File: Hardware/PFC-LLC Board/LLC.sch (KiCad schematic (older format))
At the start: 49 parts

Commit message: Updated LLC schematic
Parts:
- removed C?: C, symbol Device:C
- removed Q? (x3): BF545A, Package_TO_SOT_SMD:SOT-23, symbol Transistor_FET:BF545A
- removed U?: UCC28180DR, D8_TEX, symbol PFC_IC:UCC28180DR
- added J2, J3: Conn_01x02_Female, Connector_PinHeader_1.27mm:PinHeader_1x02_P1.27mm_Vertical, symbol Connector:Conn_01x02_Female
- added QM1, QM2: IPP060N06N, Package_TO_SOT_THT:TO-220-3_Vertical, symbol Transistor_FET:IPP060N06N
- added QM3, QM4: C2M0025120D, Package_TO_SOT_THT:TO-247-3_Vertical, symbol Transistor_FET:C2M0025120D
- added Rlimit: 18.2k, symbol Device:R
- added U1: UCC256403DDBR, SOIC14_DDB_TEX, symbol LLC_U1:UCC256403DDBR
- added U2: UCC24624DT, SOIC_4624DT_TEX, symbol LLC_U2:UCC24624DT
- added UO1: PS2501L-1-F3-A, SOIC_1L-1-A, symbol LLC_O1:PS2501L-1-F3-A
- added UVR: TLV431AIDBVT, DBV5, symbol LLC_VR:TLV431AIDBVT
- Cboot: renamed from C?; value C -> 220n
- Cbw: renamed from C?; value C -> 3.9p
- Ccomp: renamed from C?; value C -> 390n
- Cisns: renamed from C?; value C -> 3.3p
- Cout: renamed from C?; value CP -> 120u
- Coutx: renamed from C?; value C -> 22u
- Creg, Cvcc: renamed from C?; value C -> 2.2u
- Crvcc2, Cvrcc1: renamed from C?; value C -> 4.7u
- Css: renamed from C?; value C -> 47n
- Cvcc2: renamed from C?; value CP -> 15u
- Cz: renamed from C?; value C -> 100n
- Rbias: renamed from R?; value R -> 6.04k
- Rboot: renamed from R?; value R -> 2.20
- Rcomp, Rvcc1: renamed from R?; value R -> 44.2k
- Rfbb: renamed from R?; value R -> 8.06k
- Rfbt: renamed from R?; value R -> 110k
- Rled: renamed from R?; value R -> 36.5k
- Rvcc2: renamed from R?; value R -> 12.1k
- gave numbers to parts that had none: 1
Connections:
- net labels added: BLK, GND, HO, HS, LO
- wire segments 64 -> 242
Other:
- moved on the sheet: C16, Cboot, Cbw, Ccomp, Cisns, Cout, Coutx, Creg, Crvcc2, Css, Cvcc, Cvrcc1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

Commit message: Start of PCB
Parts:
- removed Cout: 120u, symbol Device:CP
- removed Css: 47n, symbol Device:C
- removed Cvcc2: 15u, symbol Device:CP
- removed Cvcr2: 1n, symbol Device:C
- removed D?: DIODE, symbol pspice:DIODE
- added Cout21, Cout22, Cout23, Cout24, Cout25, Cout26: 120u, LLC_Cout:35SVPF120M, symbol LLC_Cout:35SVPF120M
- added Coutx21, Coutx23, Coutx24: 22u, Capacitor_SMD:C_0805_2012Metric_Pad1.18x1.45mm_HandSolder, symbol Device:C
- added Css11, Css12, Css13: 47n, Capacitor_SMD:C_0402_1005Metric_Pad0.74x0.62mm_HandSolder, symbol Device:C
- added Cvcc21, Cvcc22, Cvcc23, Cvcc24, Cvcc25, Cvcc26, Cvcc27, Cvcc28: 15u, Capacitor_SMD:CP_Elec_5x5.8, symbol Device:CP
- added Cvcr21, Cvcr22, Cvcr23, Cvcr24, Cvcr25, Cvcr26: 1n, Capacitor_SMD:C_0805_2012Metric_Pad1.18x1.45mm_HandSolder, symbol Device:C
- added Dz1: BZX84Cxx, Diode_SMD:D_SOT-23_ANK, symbol Diode:BZX84Cxx
- C16: footprint (none) -> Capacitor_SMD:C_0402_1005Metric_Pad0.74x0.62mm_HandSolder
- Cboot1: renamed from Cboot; footprint (none) -> Capacitor_SMD:C_0603_1608Metric_Pad1.08x0.95mm_HandSolder
- Cbw1: renamed from Cbw; footprint (none) -> Capacitor_SMD:C_0402_1005Metric_Pad0.74x0.62mm_HandSolder
- Ccomp3: renamed from Ccomp; footprint (none) -> Capacitor_SMD:C_1206_3216Metric_Pad1.33x1.80mm_HandSolder
- Cin2: renamed from Cin; footprint (none) -> Capacitor_THT:CP_Radial_D25.0mm_P10.00mm_SnapIn
- Cinx1: renamed from Cinx; footprint (none) -> Capacitor_THT:C_Rect_L26.5mm_W10.5mm_P22.50mm_MKS4
- Cisns1: renamed from Cisns; footprint (none) -> Capacitor_SMD:C_0402_1005Metric_Pad0.74x0.62mm_HandSolder
- Cisns2: footprint (none) -> LLC_Cisns2:FA26C0G2J151JNU00; symbol Device:C -> LLC_Cisns2:FA26C0G2J151JNU00
- Coutx22: renamed from Coutx; footprint (none) -> Capacitor_SMD:C_0805_2012Metric_Pad1.18x1.45mm_HandSolder
- Cr1, Cr2: footprint (none) -> Capacitor_THT:C_Rect_L13.0mm_W5.0mm_P10.00mm_FKS3_FKP3_MKS4
- Creg1: renamed from Creg; footprint (none) -> Capacitor_SMD:C_0402_1005Metric_Pad0.74x0.62mm_HandSolder
- Crvcc2, Cvrcc1: footprint (none) -> Capacitor_SMD:C_0805_2012Metric_Pad1.18x1.45mm_HandSolder
- Cvcc3: renamed from Cvcc; footprint (none) -> Capacitor_SMD:C_0603_1608Metric_Pad1.08x0.95mm_HandSolder
- Cvcr1: footprint (none) -> Capacitor_THT:C_Rect_L7.2mm_W4.5mm_P5.00mm_FKS2_FKP2_MKS2_MKP2
- Cz1: renamed from Cz; footprint (none) -> Capacitor_SMD:C_0603_1608Metric_Pad1.08x0.95mm_HandSolder
- Dboot1: renamed from Dboot; footprint (none) -> DO-214BA:DO-214BA
- QM1, QM2: footprint Package_TO_SOT_THT:TO-220-3_Vertical -> Package_TO_SOT_THT:TO-247-3_Vertical
- R19, Rbw1, Rdrv1, Rdrv2: footprint (none) -> Resistor_SMD:R_0402_1005Metric_Pad0.72x0.64mm_HandSolder
- R20, R27, R28: footprint (none) -> Resistor_SMD:R_1206_3216Metric_Pad1.30x1.75mm_HandSolder
- Rbias1: renamed from Rbias; footprint (none) -> Resistor_SMD:R_0402_1005Metric_Pad0.72x0.64mm_HandSolder
- Rboot1: renamed from Rboot; footprint (none) -> Resistor_SMD:R_0805_2012Metric_Pad1.20x1.40mm_HandSolder
- Rbw2, Rvcc1, Rvcc2: footprint (none) -> Resistor_SMD:R_0201_0603Metric_Pad0.64x0.40mm_HandSolder
- Rcomp2: renamed from Rcomp; footprint (none) -> Resistor_SMD:R_0201_0603Metric_Pad0.64x0.40mm_HandSolder
- Rfbb2: renamed from Rfbb; footprint (none) -> Resistor_SMD:R_0402_1005Metric_Pad0.72x0.64mm_HandSolder
- Rfbt4: renamed from Rfbt; footprint (none) -> Resistor_SMD:R_0603_1608Metric_Pad0.98x0.95mm_HandSolder
- Rho1: renamed from RRho; footprint (none) -> Resistor_SMD:R_0402_1005Metric_Pad0.72x0.64mm_HandSolder
- Risns1: renamed from Risns; footprint (none) -> Resistor_SMD:R_0603_1608Metric_Pad0.98x0.95mm_HandSolder
- Rled1: renamed from Rled; footprint (none) -> Resistor_SMD:R_0201_0603Metric_Pad0.64x0.40mm_HandSolder
- Rlimit1: renamed from Rlimit; footprint (none) -> Resistor_SMD:R_1206_3216Metric_Pad1.30x1.75mm_HandSolder
- Rlo1: renamed from Rlo; footprint (none) -> Resistor_SMD:R_0402_1005Metric_Pad0.72x0.64mm_HandSolder
- U1LLC1: renamed from U1; footprint SOIC14_DDB_TEX -> LLC_U1:UCC256403DDBR
- U2LLC1: renamed from U2; footprint SOIC_4624DT_TEX -> LLC_U2:UCC24624DT
- UO1: footprint SOIC_1L-1-A -> LLC_O1:PS2501L-1-F3-A
- UVR1: renamed from UVR; footprint DBV5 -> LLC_VR1:TLV431AIDBVT
- gave numbers to parts that had none: 1
- renumbered Lr to Lr1
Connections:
- wire segments 242 -> 346
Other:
- moved on the sheet: Coutx22

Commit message: All footprints except PFC output caps
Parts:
- removed J2: Conn_01x02_Female, Connector_PinHeader_1.27mm:PinHeader_1x02_P1.27mm_Vertical, symbol Connector:Conn_01x02_Female
- removed Lr1: 37.858u, symbol pspice:INDUCTOR
- added J4, J6: 1792229, Connector2x1:PHOENIX_1792229, symbol Connector2x1:1792229
- added Lr1: PA4344.473ANLT, LLC_Lr:PA4344.473ANLT, symbol LLC_Lr:PA4344.473ANLT
- TR1: footprint (none) -> LLC_T1:EPCOS-B65982E0012D001-MFG
- renumbered J3 to J5
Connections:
- net labels added: GND1
- wire segments 346 -> 352
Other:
- moved on the sheet: Cout21, Cout22, Cout23, Cout24, Cout25, Cout26, Coutx21, Coutx22, Coutx23, Coutx24, Rfbb2, Rfbt4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

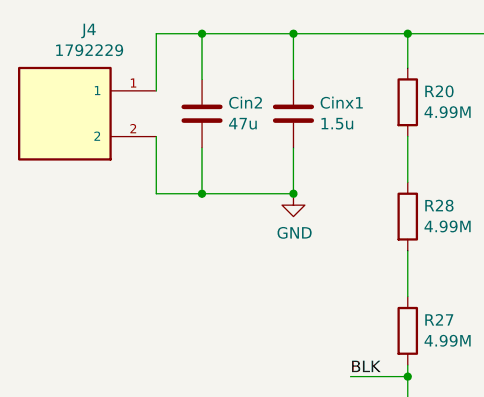
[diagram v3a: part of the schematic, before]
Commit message: layout done with some routing for LLC
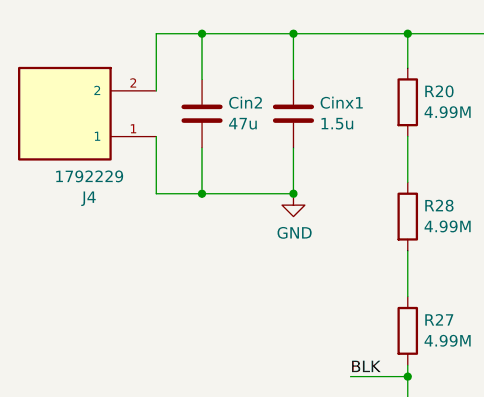
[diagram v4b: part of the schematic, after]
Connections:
- net GND: now also J4.1; no longer J4.2
- net at Cin2.1, Cinx1.1, Cr1.1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: now also J4.2; no longer J4.1
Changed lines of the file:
@@
 F 6 "Manufacturer Recommendation" H 750 1600 50  0001 L BNN "STANDARD"
 	1    750  1600
-	-1   0    0    -1
+	-1   0    0    1
 $EndComp
 Wire Wire Line
@@
 Connection ~ 14700 3250
 $Comp
-L power:GND1 #PWR?
+L power:GND1 #PWR0108
 U 1 1 609CE495
 P 15350 3250
-F 0 "#PWR?" H 15350 3000 50  0001 C CNN
+F 0 "#PWR0108" H 15350 3000 50  0001 C CNN
 F 1 "GND1" H 15355 3077 50  0000 C CNN
 F 2 "" H 15350 3250 50  0001 C CNN
@@
 Connection ~ 15350 3250
 $Comp
-L power:GND1 #PWR?
+L power:GND1 #PWR0109
 U 1 1 609D1529
 P 14250 5500
-F 0 "#PWR?" H 14250 5250 50  0001 C CNN
+F 0 "#PWR0109" H 14250 5250 50  0001 C CNN
 F 1 "GND1" H 14255 5327 50  0000 C CNN
 F 2 "" H 14250 5500 50  0001 C CNN
@@
 $EndComp
 $Comp
-L power:GND1 #PWR?
+L power:GND1 #PWR0110
 U 1 1 60A11FA4
 P 15200 7500
-F 0 "#PWR?" H 15200 7250 50  0001 C CNN
+F 0 "#PWR0110" H 15200 7250 50  0001 C CNN
 F 1 "GND1" H 15205 7327 50  0000 C CNN
 F 2 "" H 15200 7500 50  0001 C CNN

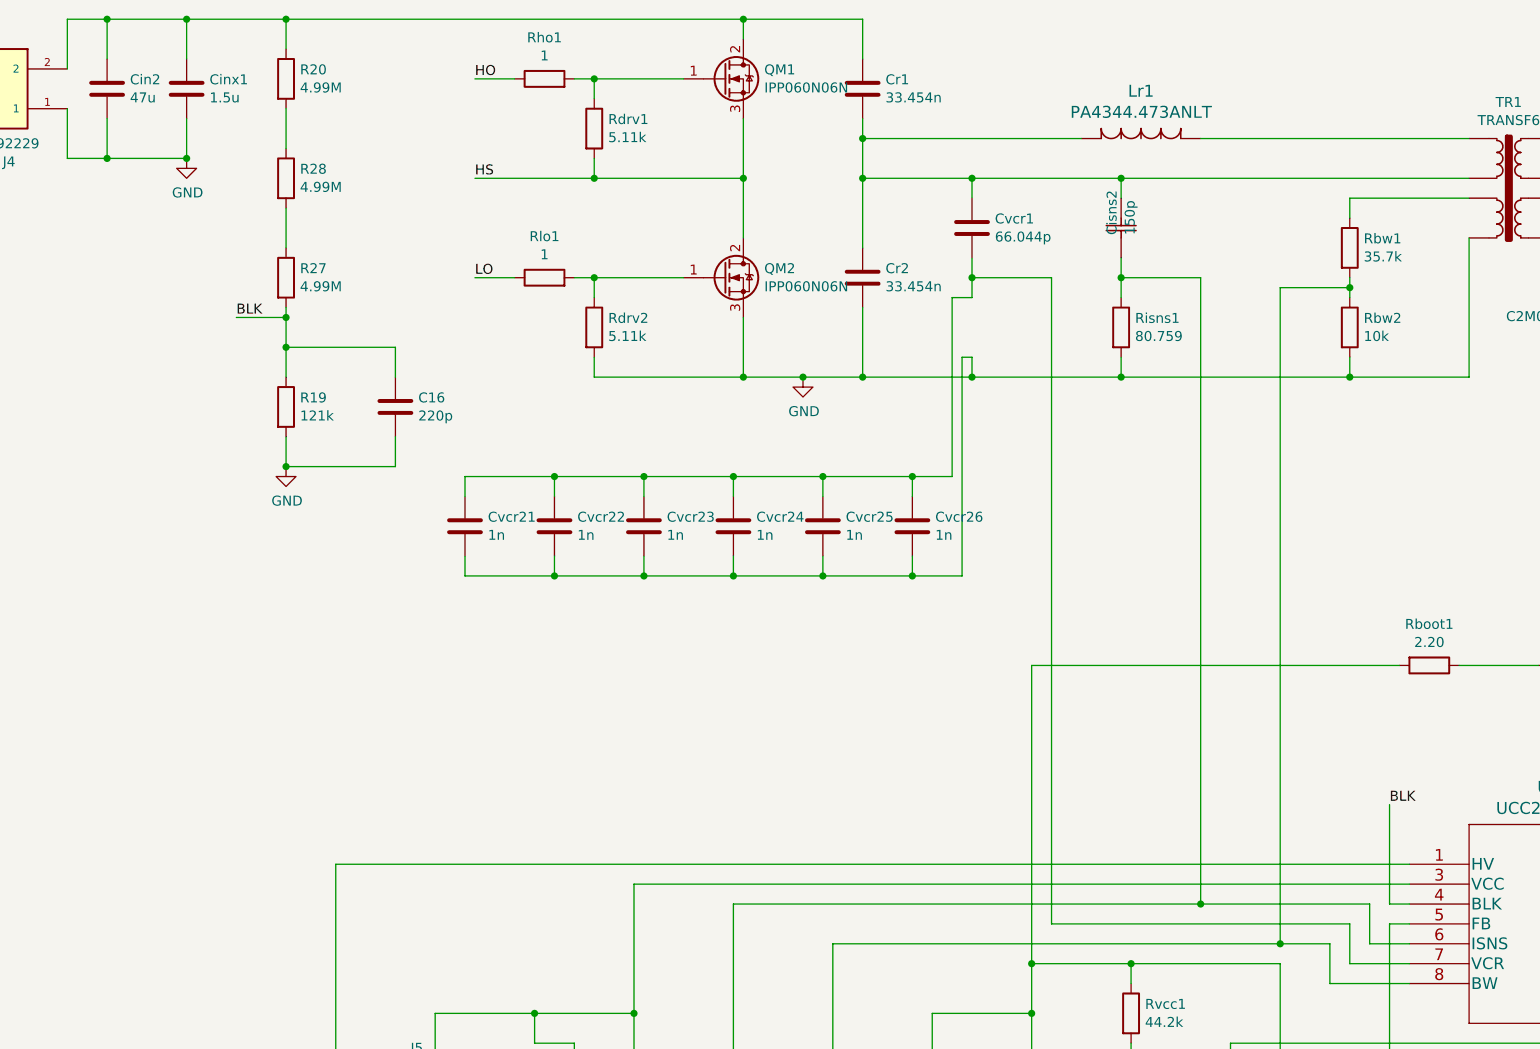
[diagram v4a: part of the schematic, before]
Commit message: PCB with flooding (expect GND)
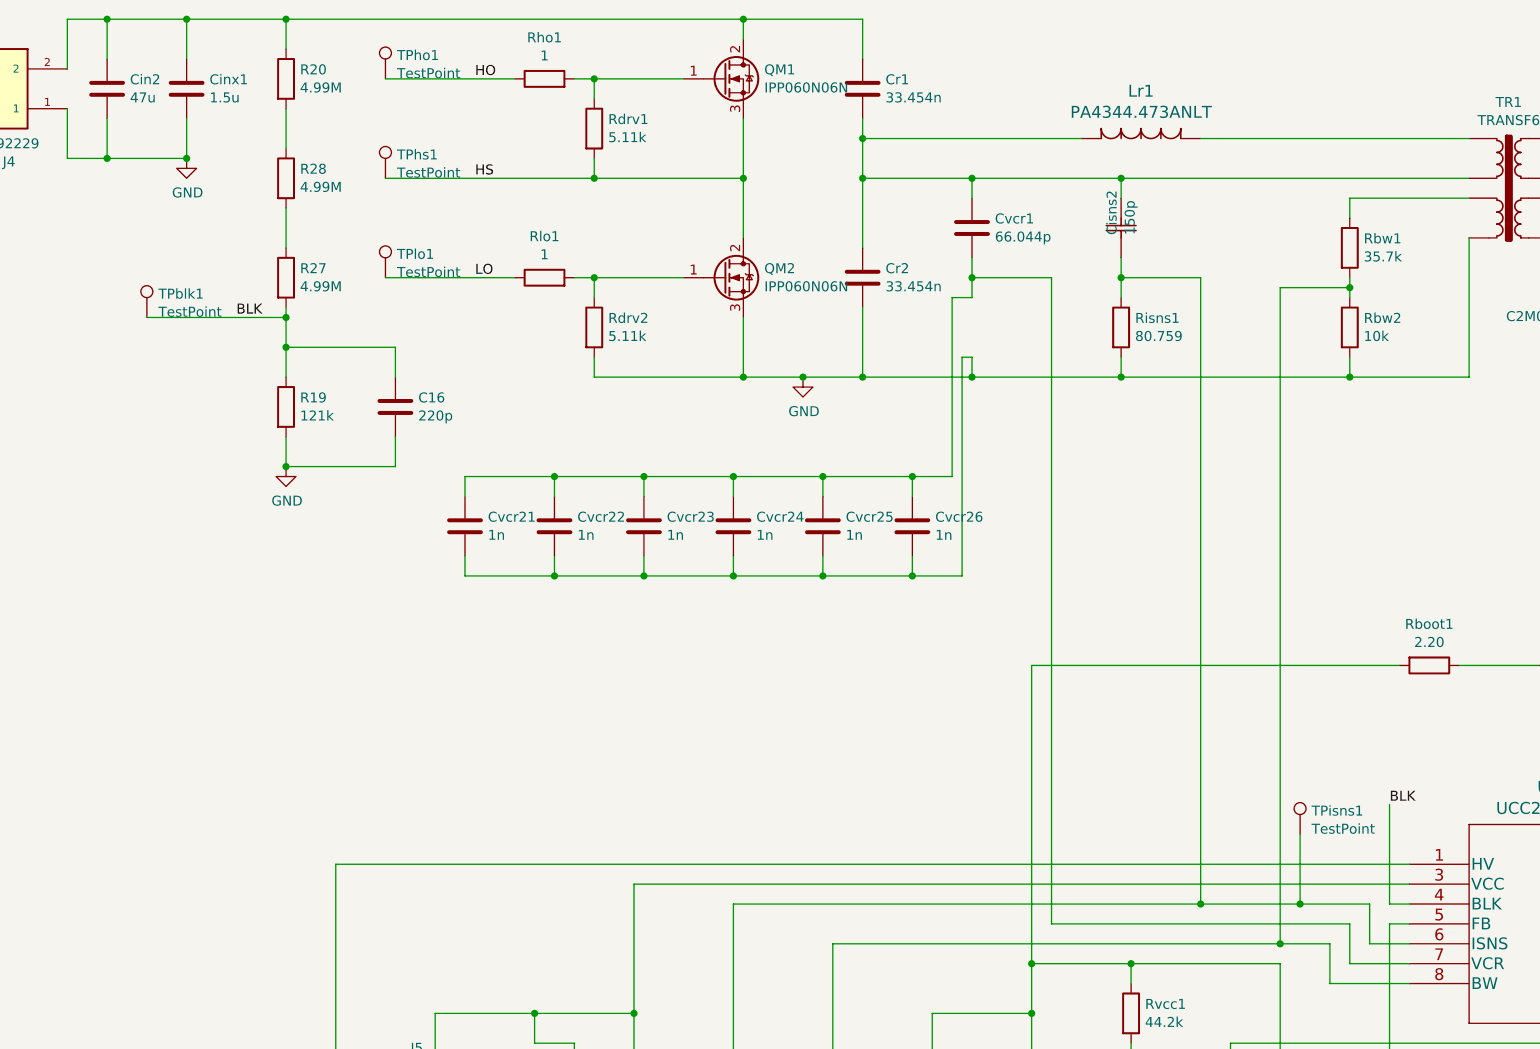
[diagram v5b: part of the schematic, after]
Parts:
- added TPblk1, TPho1, TPhs1, TPisns1, TPlo1: TestPoint, TestPoint:TestPoint_Pad_D1.0mm, symbol Connector:TestPoint
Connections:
- net BLK: now also TPblk1.1
- net HO: now also TPho1.1
- net HS: now also TPhs1.1
- net LO: now also TPlo1.1
- net at Cisns1.1, Cisns2.1, Risns1.1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: now also TPisns1.1
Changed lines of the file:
@@
 	7700 5900 7700 5700
 Wire Wire Line
-	7700 5700 6850 5700
+	7700 5700 7350 5700
 Wire Wire Line
 	4500 5700 4500 6600
@@
 Text Label 3200 1550 0    50   ~ 0
 HO
-Wire Wire Line
-	3400 1550 3200 1550
-Wire Wire Line
-	3400 2550 3200 2550
 Text Label 3200 2550 0    50   ~ 0
 LO
-Wire Wire Line
-	3800 2050 3200 2050
 Connection ~ 3800 2050
 Text Label 3200 2050 0    50   ~ 0
 HS
-Wire Wire Line
-	2250 2750 2000 2750
 Connection ~ 2250 2750
 Wire Wire Line
@@
 	13400 7500 15200 7500
 Connection ~ 15200 7500
+$Comp
+L Connector:TestPoint TPlo1
+U 1 1 604713E7
+P 2750 2550
+F 0 "TPlo1" H 2808 2668 50  0000 L CNN
+F 1 "TestPoint" H 2808 2577 50  0000 L CNN
+F 2 "TestPoint:TestPoint_Pad_D1.0mm" H 2950 2550 50  0001 C CNN
+F 3 "~" H 2950 2550 50  0001 C CNN
+	1    2750 2550
+	1    0    0    -1
+$EndComp
+$Comp
+L Connector:TestPoint TPhs1
+U 1 1 60474AAF
+P 2750 2050
+F 0 "TPhs1" H 2808 2168 50  0000 L CNN
+F 1 "TestPoint" H 2808 2077 50  0000 L CNN
+F 2 "TestPoint:TestPoint_Pad_D1.0mm" H 2950 2050 50  0001 C CNN
+F 3 "~" H 2950 2050 50  0001 C CNN
+	1    2750 2050
+	1    0    0    -1
+$EndComp
+$Comp
+L Connector:TestPoint TPho1
+U 1 1 6049555F
+P 2750 1550
+F 0 "TPho1" H 2808 1668 50  0000 L CNN
+F 1 "TestPoint" H 2808 1577 50  0000 L CNN
+F 2 "TestPoint:TestPoint_Pad_D1.0mm" H 2950 1550 50  0001 C CNN
+F 3 "~" H 2950 1550 50  0001 C CNN
+	1    2750 1550
+	1    0    0    -1
+$EndComp
+$Comp
+L Connector:TestPoint TPblk1
+U 1 1 604B5F07
+P 1550 2750
+F 0 "TPblk1" H 1608 2868 50  0000 L CNN
+F 1 "TestPoint" H 1608 2777 50  0000 L CNN
+F 2 "TestPoint:TestPoint_Pad_D1.0mm" H 1750 2750 50  0001 C CNN
+F 3 "~" H 1750 2750 50  0001 C CNN
+	1    1550 2750
+	1    0    0    -1
+$EndComp
+Wire Wire Line
+	2750 1550 3400 1550
+Wire Wire Line
+	2750 2050 3800 2050
+Wire Wire Line
+	2750 2550 3400 2550
+Wire Wire Line
+	1550 2750 2250 2750
+$Comp
+L Connector:TestPoint TPisns1
+U 1 1 6055972F
+P 7350 5350
+F 0 "TPisns1" H 7408 5468 50  0000 L CNN
+F 1 "TestPoint" H 7408 5377 50  0000 L CNN
+F 2 "TestPoint:TestPoint_Pad_D1.0mm" H 7550 5350 50  0001 C CNN
+F 3 "~" H 7550 5350 50  0001 C CNN
+	1    7350 5350
+	1    0    0    -1
+$EndComp
+Wire Wire Line
+	7350 5350 7350 5700
+Connection ~ 7350 5700
+Wire Wire Line
+	7350 5700 6850 5700
 $EndSCHEMATC

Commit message: Gerber files generated
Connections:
- net HS: now also Lr1.2
- net at Cisns2.2, Cr1.2, Cr2.1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: no longer Lr1.2
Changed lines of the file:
@@
 	6850 1850 8200 1850
-Wire Wire Line
-	5150 1750 5150 1850
 Wire Wire Line
 	8200 2050 6450 2050
@@
 $EndComp
 Wire Wire Line
-	4550 1750 4550 2050
-Wire Wire Line
-	6250 1850 5150 1850
-Connection ~ 5150 1850
-Wire Wire Line
-	5150 1850 5150 2050
+	4550 1750 4550 1850
 $Comp
 L Connector2x1:1792229 J?
@@
 Wire Wire Line
 	7350 5700 6850 5700
+Wire Wire Line
+	5150 1750 5150 2050
+Wire Wire Line
+	6250 1850 4550 1850
+Connection ~ 4550 1850
+Wire Wire Line
+	4550 1850 4550 2050
 $EndSCHEMATC

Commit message: Added Test points
Added Test points
Changed Capacitor Values around
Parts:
- C16, Cboot1, Cbw1, Ccomp3, Cin2, Cinx1, Cisns1, Coutx21, Coutx22, Coutx23, Coutx24, Cr1, Cr2, Creg1, Crvcc2, Css11, Css12, Css13, Cvcc3, Cvcr1, Cvcr21, Cvcr22, Cvcr23, Cvcr24, Cvcr25, Cvcr26, Cvrcc1, Cz1: symbol Device:C -> KiCAD-Simulations-rescue:C-Device
- Cisns2: symbol LLC_Cisns2:FA26C0G2J151JNU00 -> KiCAD-Simulations-rescue:FA26C0G2J151JNU00-LLC_Cisns2
- Cout21, Cout22, Cout23, Cout24, Cout25, Cout26: symbol LLC_Cout:35SVPF120M -> KiCAD-Simulations-rescue:35SVPF120M-LLC_Cout
- Cvcc21, Cvcc22, Cvcc23, Cvcc24, Cvcc25, Cvcc26, Cvcc27, Cvcc28: symbol Device:CP -> KiCAD-Simulations-rescue:CP-Device
- Dboot1: symbol pspice:DIODE -> KiCAD-Simulations-rescue:DIODE-pspice
- Dz1: symbol Diode:BZX84Cxx -> KiCAD-Simulations-rescue:BZX84Cxx-Diode
- J4, J6: symbol Connector2x1:1792229 -> KiCAD-Simulations-rescue:1792229-Connector2x1
- J5: symbol Connector:Conn_01x02_Female -> KiCAD-Simulations-rescue:Conn_01x02_Female-Connector
- Lr1: symbol LLC_Lr:PA4344.473ANLT -> KiCAD-Simulations-rescue:PA4344.473ANLT-LLC_Lr
- QM1, QM2: symbol Transistor_FET:IPP060N06N -> KiCAD-Simulations-rescue:IPP060N06N-Transistor_FET
- QM3, QM4: symbol Transistor_FET:C2M0025120D -> KiCAD-Simulations-rescue:C2M0025120D-Transistor_FET
- R19, R20, R27, R28, Rbias1, Rboot1, Rbw1, Rbw2, Rcomp2, Rdrv1, Rdrv2, Rfbb2, Rfbt4, Rho1, Risns1, Rled1, Rlimit1, Rlo1, Rvcc1, Rvcc2: symbol Device:R -> KiCAD-Simulations-rescue:R-Device
- TPblk1, TPho1, TPhs1, TPisns1, TPlo1: symbol Connector:TestPoint -> KiCAD-Simulations-rescue:TestPoint-Connector
- TR1: symbol Transformer:TRANSF6 -> KiCAD-Simulations-rescue:TRANSF6-Transformer
- U1LLC1: symbol LLC_U1:UCC256403DDBR -> KiCAD-Simulations-rescue:UCC256403DDBR-LLC_U1
- U2LLC1: symbol LLC_U2:UCC24624DT -> KiCAD-Simulations-rescue:UCC24624DT-LLC_U2
- UO1: symbol LLC_O1:PS2501L-1-F3-A -> KiCAD-Simulations-rescue:PS2501L-1-F3-A-LLC_O1
- UVR1: symbol LLC_VR:TLV431AIDBVT -> KiCAD-Simulations-rescue:TLV431AIDBVT-LLC_VR
